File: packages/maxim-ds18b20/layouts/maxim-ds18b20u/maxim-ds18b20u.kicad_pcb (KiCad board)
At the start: 2 copper layers, 2 parts

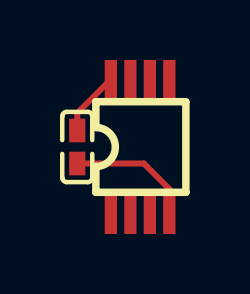
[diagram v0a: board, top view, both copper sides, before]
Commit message: Upgrade Packages: Narayans Half (#185)
* adi-ad5693r

* fix frozen

* prjc-teensy_4_1

* rp2040

* adi-adxl375: Add missing usage build target to ato.yaml

* adi-ds2482s-800: Update layout files after build

* adi-ltc4311: Update layout to fix frozen build

- Updated net names (BUS1/BUS2 → SDA/SCL, gnd → GND, hv → VCC)
- Fixed footprint properties and coordinates
- Package now passes frozen build and verification

* awinic-aw9523: Update layout to fix frozen build

- Updated net names (AD0/AD1 → address_bit_0/address_bit_1, hv → VCC, gnd → GND)
- Updated GPIO line names (-line-0 → gpios[8]-line, etc.)
- Fixed footprint properties and coordinates
- Package now passes frozen build and verification

* awinic-aw9523: Bump version to 0.1.1

- Version bump due to layout updates to fix frozen build

* adi-adbms6830: Fix package verify issues

- Add has_part_removed trait to components missing pickers (atopile_logo, SPDT, analog_DPDT)
- Add missing import for has_part_removed trait
- Add exclude_checks to usage build in ato.yaml
- Update README.md to match usage.ato content
- Bump version from 0.1.2 to 0.1.3

Package now passes ato package verify -s

* indicator-leds: Update layout and bump version

- Updated PCB layout coordinates to fix frozen build issues
- Bumped version from 0.1.5 to 0.1.6
- Package now passes ato package verify -s successfully

* Bump package versions for done packages

- adi-adxl345: 0.1.1 -> 0.1.2
- adi-adxl375: 0.1.0 -> 0.1.1
- adi-ds2482s-800: 0.1.0 -> 0.1.1
- adi-ltc4311: 0.1.0 -> 0.1.1
- adi-ltc4316: 0.1.0 -> 0.1.1
- ams-tsl2591: 0.1.0 -> 0.1.1

These packages were marked as 'Done' in package-todos.md but had version
warnings during package verification. Version bumps ensure they can be
published to the registry.

* invensense-mpu6050: Update layout files and bump version to 0.1.2

* Fix picker warnings by adding has_part_removed trait to MCU modules

- Added #pragma experiment("TRAITS") to enable traits feature
- Added import has_part_removed t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
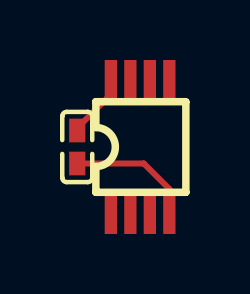
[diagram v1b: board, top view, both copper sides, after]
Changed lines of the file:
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@@
             )
         )
-        (property "__atopile_lib_fp_hash__" "5469c501-fbc2-0420-9000-686e850ba997"
+        (property "__atopile_lib_fp_hash__" "c18269d2-959d-2f4b-bc19-894555cc8b14"
             (at 0 0 0)
             (layer "User.9")
@@
         )
         (fp_text user "${REFERENCE}"
+            (at 0 -6.25 0)
+            (layer "F.SilkS")
+            (hide yes)
+            (effects
+                (font
+                    (size 1 1)
+                    (thickness 0.15)
+                )
+                (hide yes)
+            )
+            (unlocked no)
+        )
+        (fp_text user "${REFERENCE}"
             (at 0 0 0)
             (layer "F.Fab")
@@
         (at -2.1 0 -90)
         (property "Reference" "C1"
-            (at 0 -4 90)
+            (at 0 -4 0)
             (layer "F.SilkS")
             (hide yes)
@@
         )
         (property "Value" "100nF ±10% 16V X7R"
-            (at 0 4 90)
+            (at 0 4 0)
             (layer "F.Fab")
             (hide no)
@@
         )
         (property "checksum" "dee2f3e8b3b5dcf7b72bbcb4e8c6e40185d754e15ce4224dccbc55d9ddeb3abe"
-            (at 0 0 90)
-            (layer "User.9")
-            (hide yes)
-            (effects
-                (font
-                    (size 0.125 0.125)
-                    (thickness 0.01875)
-                )
-            )
-        )
-        (property "__atopile_lib_fp_hash__" "abd85f6b-95fa-ed5a-88fe-be39d3a76574"
-            (at 0 0 90)
+            (at 0 0 0)
+            (layer "User.9")
+            (hide yes)
+            (effects
+                (font
+                    (size 0.125 0.125)
+                    (thickness 0.01875)
+                )
+            )
+        )
+        (property "__atopile_lib_fp_hash__" "f8a97365-7255-729e-24e5-6102db053d76"
+            (at 0 0 0)
             (layer "User.9")
             (hide yes)
@@
         )
         (fp_text user "${REFERENCE}"
-            (at 0 0 90)
+            (at 0 -4 0)
+            (layer "F.SilkS")
+            (hide yes)
+            (effects
+                (font
+                    (size 1 1)
+                    (thickness 0.15)
+                )
+                (hide yes)
+            )
+            (unlocked no)
+        )
+        (fp_text user "${REFERENCE}"
+            (at 0 0 0)
             (layer "F.Fab")
             (effects
@@
     )
     (segment
-        (start -2.1 -1.13)
+        (start -2.1 -0.632)
         (end -2.1 -0.55)
         (width 0.2)
@@
     (segment
         (start -0.98 -2.25)
-        (end -2.1 -1.13)
+        (end -0.98 -1.752)
         (width 0.2)
         (net 8)
+        (layer "F.Cu")
+    )
+    (segment
+        (start -0.98 -1.752)
+        (end -2.1 -0.632)
+        (width 0.2)
+        (net 8)

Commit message: review tool updates
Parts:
- C1: value 100nF ±10% 16V X7R -> 1.0000000000000001e-07F
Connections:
- net GND renamed lv
- net VCC renamed hv
- U1 pad 2: footprint-net-0 -> (no net)
- U1 pad 3: footprint-net-1 -> (no net)
- U1 pad 5: footprint-net-2 -> (no net)
- U1 pad 6: footprint-net-3 -> (no net)
- U1 pad 7: footprint-net-4 -> (no net)

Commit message: maxim-ds18b20: sync build outputs
Build targets:
  default = rc0
  maxim-ds18b20 = rc0
  maxim-ds18b20u = rc0
  maxim-ds18b20z = rc0
  usage = rc0
Package Verify: rc0
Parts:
- C1: value 1.0000000000000001e-07F -> [capacitance: unknown]
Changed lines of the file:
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@@
 			)
 		)
-		(property "Value" "1.0000000000000001e-07F"
+		(property "Value" "[capacitance: unknown]"
 			(at 0 4 270)
 			(layer "F.Fab")
@@
 			)
 		)
-		(property "capacitance" "1.0000000000000001e-07±10.0%F"
+		(property "capacitance" "[capacitance: unknown]"
 			(at 0 0 0)
 			(layer "User.9")
 			(hide yes)
 		)
-		(property "max_voltage" "16.0V"
+		(property "max_voltage" "[max_voltage: unknown]"
 			(at 0 0 0)
 			(layer "User.9")
 			(hide yes)
 		)
-		(property "temperature_coefficient" "X7R"
+		(property "temperature_coefficient" "[temperature_coefficient: unknown]"
 			(at 0 0 0)
 			(layer "User.9")
